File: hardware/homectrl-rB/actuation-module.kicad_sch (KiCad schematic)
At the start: 0 parts

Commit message: stepper driver circuitry
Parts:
- added C27: 2.2uF 6.3V, symbol Device:C
- added C28: 0.1uF 10V, symbol Device:C
- added C29: 22nF 50V, symbol Device:C
- added C30: 4.7uF 6.3V, symbol Device:C
- added C31, C32, C34: 0.1uF 24V, symbol Device:C
- added C33: 100uF 24V, symbol Device:C
- added D12, D13: S1M, symbol Device:D
- added J6: PUMP0-CONN, symbol Connector_Generic:Conn_01x02
- added J7: PUMP1-CONN, symbol Connector_Generic:Conn_01x02
- added J8: STEP-CONN, symbol Connector_Generic:Conn_01x04
- added Q2, Q3: IRLZ44N, IRLZ44N:TO254P1054X469X1930-3, symbol IRLZ44N:IRLZ44N
- added R21, R23, R27: 1k, symbol Device:R
- added R22, R24: 10k, symbol Device:R
- added R25, R26: 0.11, symbol Device:R
- added U8: TMC2209, QFN28_5X5_TRI, symbol TMC2209:TMC2209
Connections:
- new net: Q3.1, R23.2, R24.2
- new net: Q2.1, R21.2, R22.2
- new net: C29.1, U8.4 (CPO)
- new net: C29.2, U8.5 (CPI)
- new net: C27.1, C30.1, U8.8 (5VOUT)
- new net: R26.1, U8.23 (BRA)
- new net: R25.1, U8.27 (BRB)
- new net +12V: C31.1, C32.1, C33.1, C34.2, D12.1 (K), D13.1 (K), J6.1 (Pin_1), J7.1 (Pin_1), U8.22 (VS), U8.28 (VS), U8.6 (VCP)
- new net +3V3: C28.2, U8.10 (MS2_AD1), U8.15 (VCC_IO), U8.9 (MS1_AD0)
- new net 1A: J8.1 (Pin_1), U8.24 (OA1)
- new net 1B: J8.2 (Pin_2), U8.26 (OB1)
- new net 2A: J8.3 (Pin_3), U8.21 (OA2)
- new net 2B: J8.4 (Pin_4), U8.1 (OB2)
- new net DIR: U8.19 (DIR)
- new net ENN: U8.2 (ENN)
- new net GND: C27.2, C28.1, C30.2, C31.2, C32.2, C33.2, C34.1, Q2.3, Q3.3, R22.1, R24.1, R25.2, R26.2, U8.13 (CLK), U8.18 (GND), U8.29 (GND), U8.3 (GND), U8.7 (SPREAD)
- new net PGATE-0: R21.1
- new net PGATE-1: R23.1
- new net PUMP0-N: D12.2 (A), J6.2 (Pin_2), Q2.2
- new net PUMP1-N: D13.2 (A), J7.2 (Pin_2), Q3.2
- new net S3-RX: R27.2
- new net S3-TX: R27.1, U8.14 (PDN_UART)
- new net STEP: U8.16 (STEP)
- no-connect marks 0 -> 4
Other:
- note added: "+"
- note added: "-"
- note added: "A-IN"
- note added: "A-SW"
- note added: "STEP-DRV"

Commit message: assign footprints
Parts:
- C27: value 2.2uF 6.3V -> 2.2uF 10V; footprint (none) -> Capacitor_SMD:C_0201_0603Metric
- C28, C29: footprint (none) -> Capacitor_SMD:C_0603_1608Metric
- C30: value 4.7uF 6.3V -> 4.7uF 10V; footprint (none) -> Capacitor_SMD:C_0805_2012Metric
- C31, C32, C34: value 0.1uF 24V -> 0.1uF 50V; footprint (none) -> Capacitor_SMD:C_0603_1608Metric
- C33: value 100uF 24V -> 100uF 50V; footprint (none) -> Capacitor_SMD:CP_Elec_6.3x5.4
- D12: value S1M -> P0D; footprint (none) -> Diode_SMD:D_SMA
- D13: value S1M -> P1D; footprint (none) -> Diode_SMD:D_SMA
- J6, J7: footprint (none) -> 530480210:MOLEX_530480210
- J8: footprint (none) -> 530480410:MOLEX_530480410
- R21, R22, R23, R24: footprint (none) -> Resistor_SMD:R_0603_1608Metric
- R25, R26: footprint (none) -> Resistor_SMD:R_1206_3216Metric
- R27: footprint (none) -> Resistor_SMD:R_0402_1005Metric
- U8: footprint QFN28_5X5_TRI -> ul_TMC2209:QFN28_5X5_TRI
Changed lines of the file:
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@@
 			)
 		)
-		(property "Value" "S1M"
+		(property "Value" "P0D"
 			(at 39.37 38.1 0)
 			(effects
@@
 			)
 		)
-		(property "Footprint" ""
+		(property "Footprint" "Diode_SMD:D_SMA"
 			(at 39.37 41.91 0)
 			(effects
@@
 			)
 		)
-		(property "Footprint" ""
+		(property "Footprint" "Resistor_SMD:R_0603_1608Metric"
 			(at 87.63 65.278 90)
 			(effects
@@
 			)
 		)
-		(property "Footprint" ""
+		(property "Footprint" "Resistor_SMD:R_0603_1608Metric"
 			(at 41.91 65.278 90)
 			(effects
@@
 			)
 		)
-		(property "Footprint" ""
+		(property "Footprint" "Capacitor_SMD:C_0603_1608Metric"
 			(at 119.6848 142.24 0)
 			(effects
@@
 			)
 		)
-		(property "Value" "0.1uF 24V"
+		(property "Value" "0.1uF 50V"
 			(at 153.924 125.984 0)
 			(effects
@@
 			)
 		)
-		(property "Footprint" ""
+		(property "Footprint" "Capacitor_SMD:C_0603_1608Metric"
 			(at 155.9052 121.92 0)
 			(effects
@@
 			)
 		)
-		(property "Footprint" ""
+		(property "Footprint" "Resistor_SMD:R_0603_1608Metric"
 			(at 43.688 69.85 90)
 			(effects
@@
 			)
 		)
-		(property "Footprint" ""
+		(property "Footprint" "Capacitor_SMD:C_0603_1608Metric"
 			(at 58.1152 116.84 0)
 			(effects
@@
 			)
 		)
-		(property "Value" "0.1uF 24V"
+		(property "Value" "0.1uF 50V"
 			(at 142.748 125.984 0)
 			(effects
@@
 			)
 		)
-		(property "Footprint" ""
+		(property "Footprint" "Capacitor_SMD:C_0603_1608Metric"
 			(at 145.7452 121.92 0)
 			(effects
@@
 			)
 		)
-		(property "Value" "S1M"
+		(property "Value" "P1D"
 			(at 71.12 38.1 0)
 			(effects
@@
 			)
 		)
-		(property "Footprint" ""
+		(property "Footprint" "Diode_SMD:D_SMA"
 			(at 71.12 41.91 0)
 			(effects
@@
 			)
 		)
-		(property "Footprint" ""
+		(property "Footprint" "Resistor_SMD:R_0603_1608Metric"
 			(at 89.408 69.85 90)
 			(effects
@@
 			)
 		)
-		(property "Value" "2.2uF 6.3V"
+		(property "Value" "2.2uF 10V"
 			(at 37.338 126.238 0)
 			(effects
@@
 			)
 		)
-		(property "Footprint" ""
+		(property "Footprint" "Capacitor_SMD:C_0201_0603Metric"
 			(at 51.7652 129.54 0)
 			(effects
@@
 			)
 		)
-		(property "Footprint" ""
+		(property "Footprint" "530480210:MOLEX_530480210"
 			(at 69.85 27.94 0)
 			(effects
@@
 			)
 		)
-		(property "Footprint" ""
+		(property "Footprint" "530480410:MOLEX_530480410"
 			(at 101.6 27.94 0)
 			(effects
@@
 			)
 		)
-		(property "Value" "100uF 24V"
+		(property "Value" "100uF 50V"
 			(at 168.656 119.38 0)
 			(effects
@@
 			)
 		)
-		(property "Footprint" ""
+		(property "Footprint" "Capacitor_SMD:CP_Elec_6.3x5.4"
 			(at 166.0652 121.92 0)
 			(effects
@@
 			)
 		)
-		(property "Value" "0.1uF 24V"
+		(property "Value" "0.1uF 50V"
 			(at 33.528 113.538 0)
 			(effects
@@
 			)
 		)
-		(property "Footprint" ""
+		(property "Footprint" "Capacitor_SMD:C_0603_1608Metric"
 			(at 47.9552 116.84 0)
 			(effects
@@
 			)
 		)
-		(property "Footprint" ""
+		(property "Footprint" "530480210:MOLEX_530480210"
 			(at 38.1 27.94 0)
 			(effects
@@
 			)
 		)
-		(property "Footprint" "QFN28_5X5_TRI"
+		(property "Footprint" "ul_TMC2209:QFN28_5X5_TRI"
 			(at 69.85 104.14 0)
 			(effects
@@
 			)
 		)
-		(property "Footprint" ""
+		(property "Footprint" "Resistor_SMD:R_1206_3216Metric"
 			(at 124.46 121.158 90)
 			(effects
@@
 			)
 		)
-		(property "Footprint" ""
+		(property "Footprint" "Resistor_SMD:R_0402_1005Metric"
 			(at 59.182 140.97 90)
 			(effects
@@
 			)
 		)
-		(property "Value" "4.7uF 6.3V"
+		(property "Value" "4.7uF 10V"
 			(at 37.084 131.572 0)
 			(effects
@@
 			)
 		)
-		(property "Footprint" ""
+		(property "Footprint" "Capacitor_SMD:C_0805_2012Metric"
 			(at 58.1152 129.54 0)
 			(effects
@@
 			)
 		)
-		(property "Footprint" ""
+		(property "Footprint" "Resistor_SMD:R_1206_3216Metric"
 			(at 124.46 110.998 90)
 			(effects

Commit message: layout work
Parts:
- C27: footprint Capacitor_SMD:C_0201_0603Metric -> Capacitor_SMD:C_0603_1608Metric
- Q2, Q3: footprint IRLZ44N:TO254P1054X469X1930-3 -> Package_TO_SOT_SMD:SOT-23
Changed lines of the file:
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@@
 			)
 		)
-		(property "Footprint" "IRLZ44N:TO254P1054X469X1930-3"
+		(property "Footprint" "Package_TO_SOT_SMD:SOT-23"
 			(at 48.26 60.96 0)
 			(effects
@@
 			)
 		)
-		(property "Footprint" "Capacitor_SMD:C_0201_0603Metric"
+		(property "Footprint" "Capacitor_SMD:C_0603_1608Metric"
 			(at 51.7652 129.54 0)
 			(effects
@@
 			)
 		)
-		(property "Footprint" "IRLZ44N:TO254P1054X469X1930-3"
+		(property "Footprint" "Package_TO_SOT_SMD:SOT-23"
 			(at 93.98 60.96 0)
 			(effects

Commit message: W
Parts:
- C27, C28, C29, C30, C31, C32, C33, C34, D12, D13, Q2, Q3, U8: Purchase (none) -> Yes
- J6, J7, J8: Purchase (none) -> No
- R21, R22, R23, R24, R25, R26, R27: Purchase (none) -> N/A

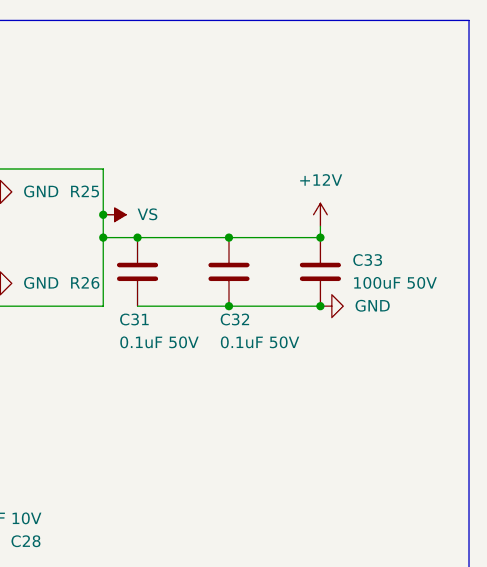
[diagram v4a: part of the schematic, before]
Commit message: add new caps, add ferrite bead, add MPNs
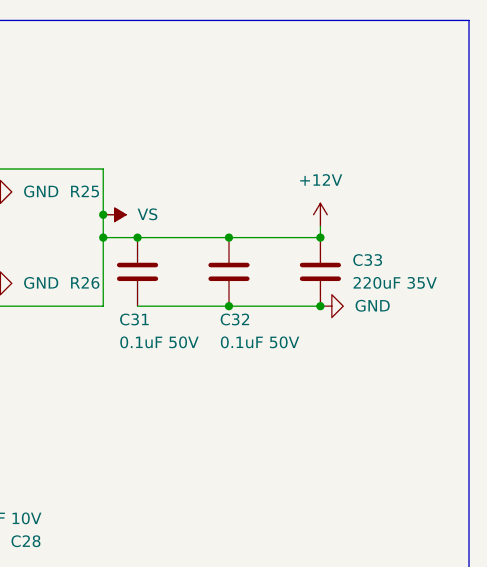
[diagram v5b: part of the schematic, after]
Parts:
- C33: value 100uF 50V -> 220uF 35V; footprint Capacitor_SMD:CP_Elec_6.3x5.4 -> EEE_FK1V101P:CAP_EEEFK1V101P; MPN (none) -> EEE-FK1V221P
- J6, J7, J8: MPN (none) -> N/A
- R21, R22, R23, R24, R25, R26, R27: Purchase N/A -> Yes
- U8: MPN (none) -> TMC2209-LA-T
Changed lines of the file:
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@@
 			)
 		)
-		(property "Purchase" "N/A"
+		(property "Purchase" "Yes"
 			(at 87.63 63.5 0)
 			(effects
@@
 			)
 		)
-		(property "Purchase" "N/A"
+		(property "Purchase" "Yes"
 			(at 41.91 63.5 0)
 			(effects
@@
 			)
 		)
-		(property "Purchase" "N/A"
+		(property "Purchase" "Yes"
 			(at 41.91 69.85 0)
 			(effects
@@
 			)
 		)
-		(property "Purchase" "N/A"
+		(property "Purchase" "Yes"
 			(at 87.63 69.85 0)
 			(effects
@@
 			)
 		)
-		(property "MPN" ""
+		(property "MPN" "N/A"
 			(at 69.85 27.94 0)
 			(effects
@@
 			)
 		)
-		(property "MPN" ""
+		(property "MPN" "N/A"
 			(at 101.6 27.94 0)
 			(effects
@@
 			)
 		)
-		(property "Value" "100uF 50V"
+		(property "Value" "220uF 35V"
 			(at 168.656 119.38 0)
 			(effects
@@
 			)
 		)
-		(property "Footprint" "Capacitor_SMD:CP_Elec_6.3x5.4"
+		(property "Footprint" "EEE_FK1V101P:CAP_EEEFK1V101P"
 			(at 166.0652 121.92 0)
 			(effects
@@
 			)
 		)
-		(property "MPN" ""
+		(property "MPN" "EEE-FK1V221P"
 			(at 165.1 118.11 0)
 			(effects
@@
 			)
 		)
-		(property "MPN" ""
+		(property "MPN" "N/A"
 			(at 38.1 27.94 0)
 			(effects
@@
 			)
 		)
-		(property "MPN" ""
+		(property "MPN" "TMC2209-LA-T"
 			(at 69.85 104.14 0)
 			(effects
@@
 			)
 		)
-		(property "Purchase" "N/A"
+		(property "Purchase" "Yes"
 			(at 124.46 119.38 0)
 			(effects
@@
 			)
 		)
-		(property "Purchase" "N/A"
+		(property "Purchase" "Yes"
 			(at 60.96 140.97 0)
 			(effects
@@
 			)
 		)
-		(property "Purchase" "N/A"
+		(property "Purchase" "Yes"
 			(at 124.46 109.22 0)
 			(effects

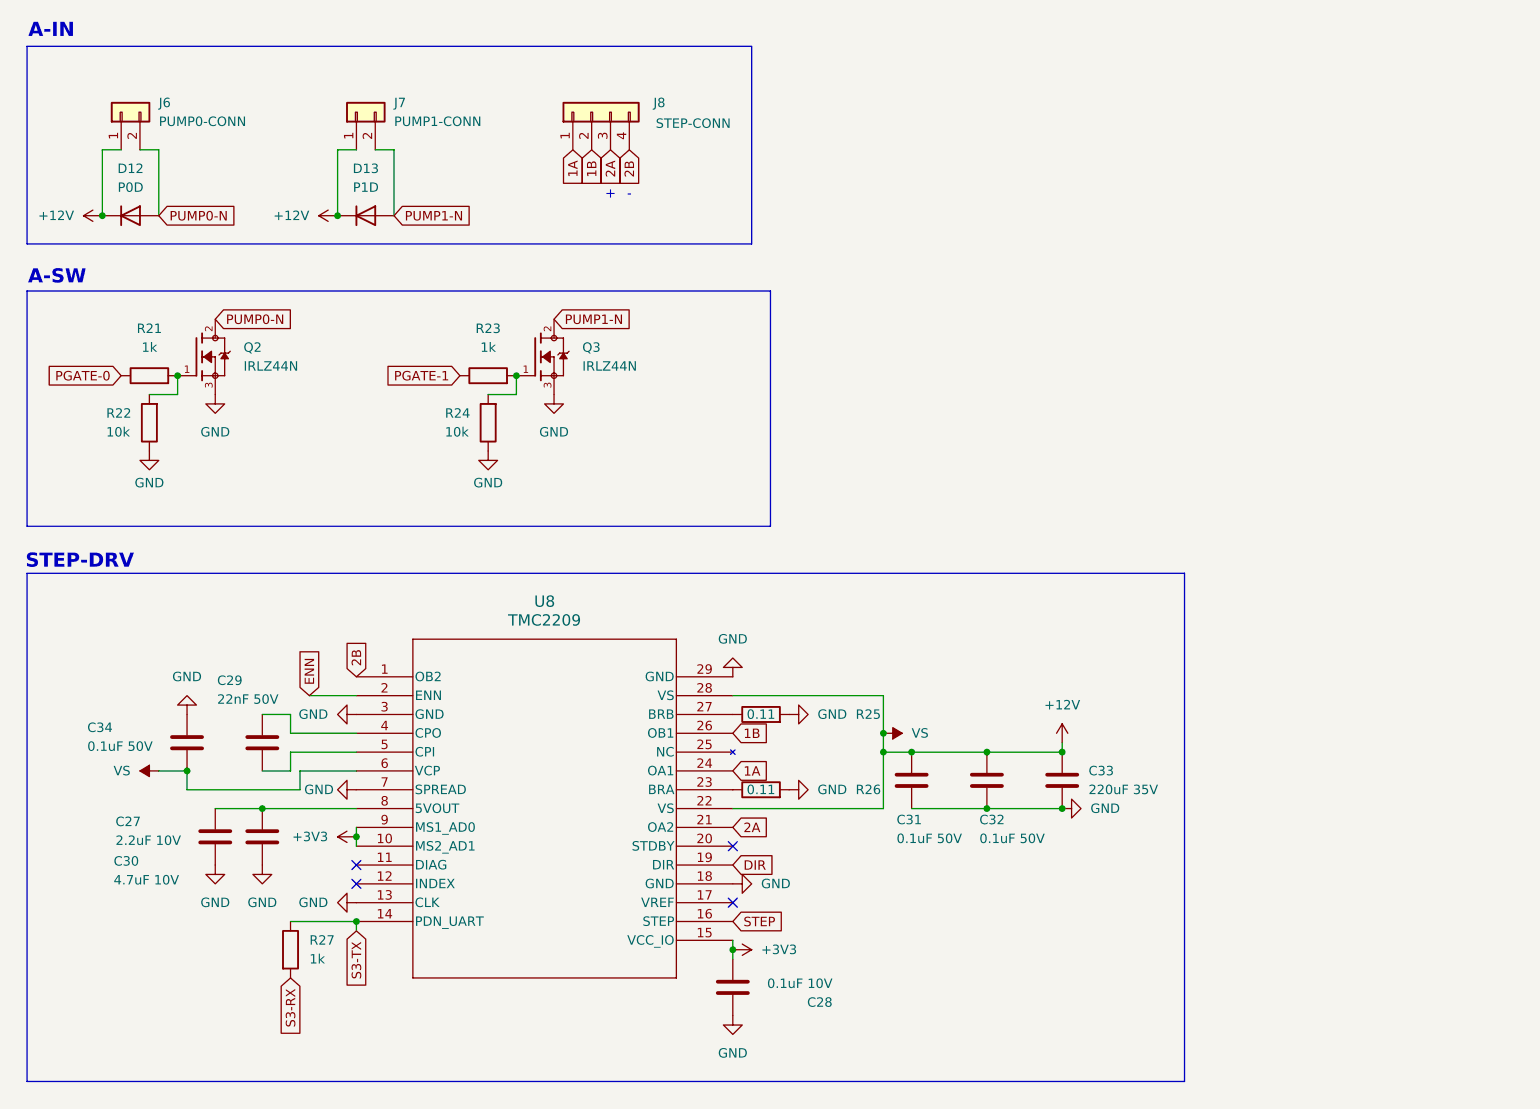
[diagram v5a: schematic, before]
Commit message: add MPNs and review circuits
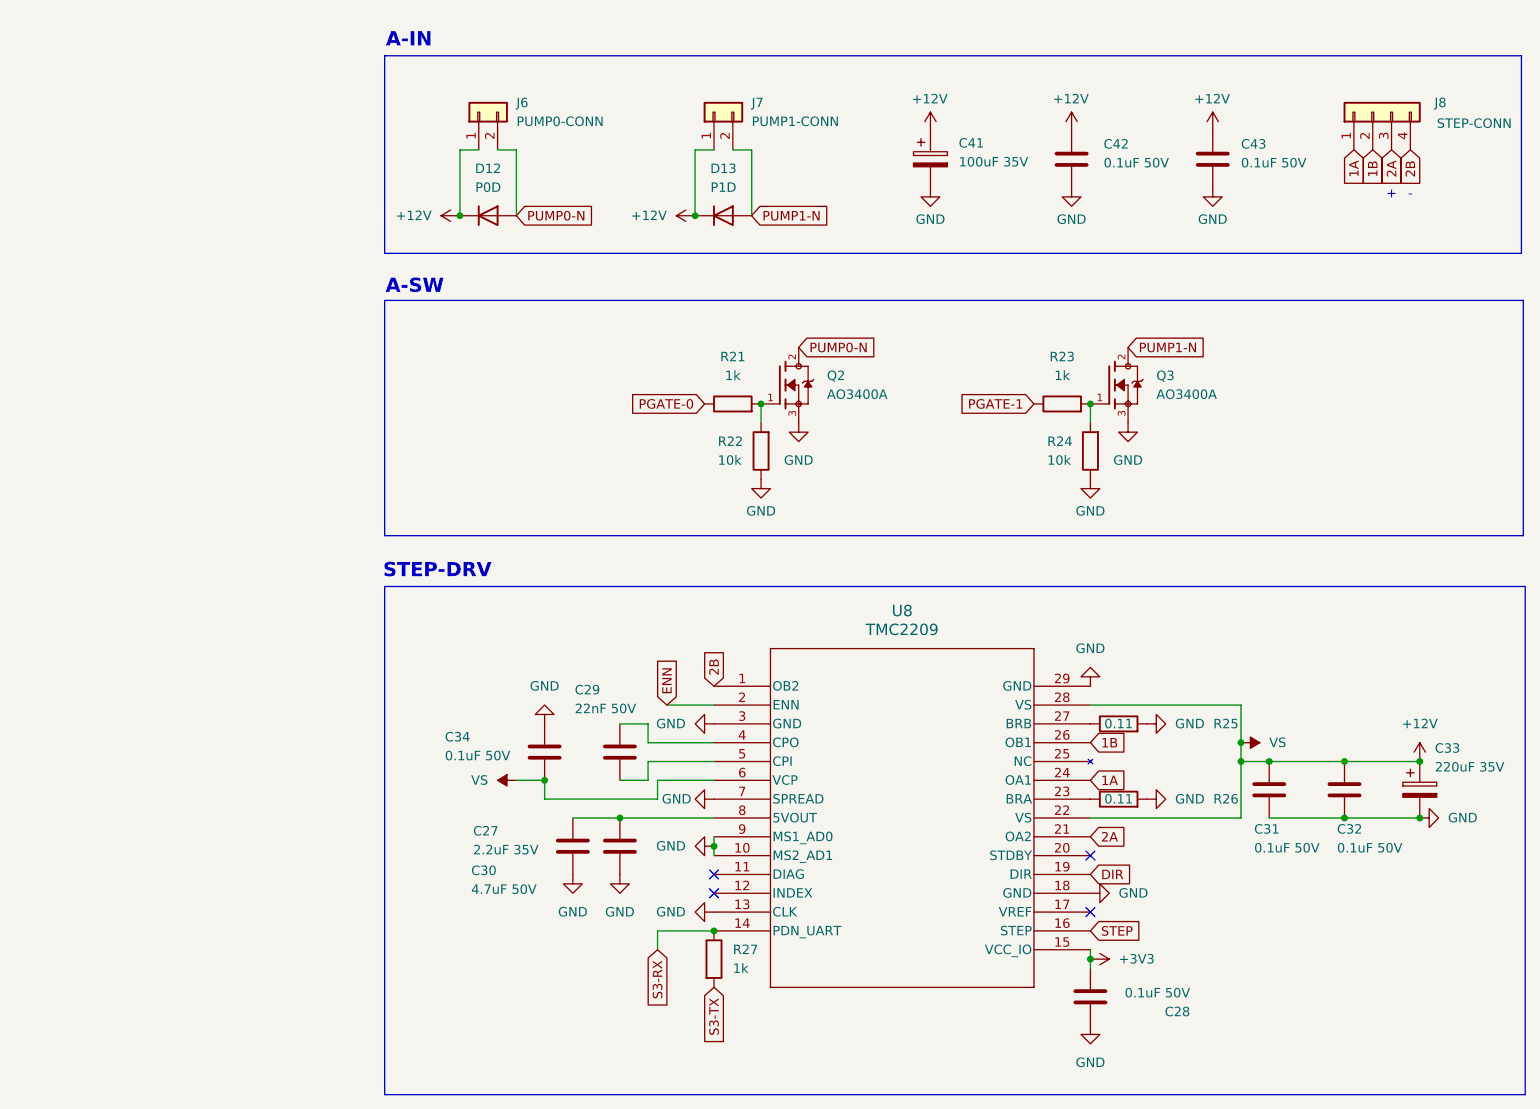
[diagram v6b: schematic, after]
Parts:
- added C41: 100uF 35V, EEH_ZK1V101XP:CAP_EEHZK1V101XP, symbol Device:C_Polarized
- added C42, C43: 0.1uF 50V, Capacitor_SMD:C_0603_1608Metric, symbol Device:C
- C27: value 2.2uF 10V -> 2.2uF 35V; MPN (none) -> https://www.digikey.ca/en/products/detail/murata-electronic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
- C28: value 0.1uF 10V -> 0.1uF 50V; MPN (none) -> GRM188R71H104KA93D
- C29: MPN (none) -> CL10B223KB8NNNC
- C30: value 4.7uF 10V -> 4.7uF 50V; MPN (none) -> CL21A475KBQNNNE
- C31, C32, C34: MPN (none) -> GRM188R71H104KA93D
- C33: symbol Device:C -> Device:C_Polarized
- D12, D13: MPN (none) -> SS14
- Q2: value IRLZ44N -> AO3400A; MPN (none) -> AO3400A
- Q3: value IRLZ44N -> AO3400A; MP IRLZ44N -> (none); MPN (none) -> AO3400A
- R21: MPN (none) -> ERJ-3EKF1001V
- R22, R24: MPN (none) -> ERJ-3EKF1002V
- R23: MPN (none) -> https://industrial.panasonic.com/cdbs/www-data/pdf/RDA0000/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
- R25, R26: MPN (none) -> RL1206FR-070R11L
- R27: MPN (none) -> ERJ-2RKF1001X
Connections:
- net +12V: now also C41.1, C42.1, C43.1
- net +3V3: no longer U8.10 (MS2_AD1), U8.9 (MS1_AD0)
- net GND: now also U8.10 (MS2_AD1), U8.9 (MS1_AD0), C41.2, C42.2, C43.2
- net S3-RX: now also R27.1, U8.14 (PDN_UART); no longer R27.2
- net S3-TX: now also R27.2; no longer R27.1, U8.14 (PDN_UART)
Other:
- moved on the sheet: C27, C28, C29, C30, C31, C32, C34, D12, D13, J6, J7, J8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

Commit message: pad clearance & BOM fixes
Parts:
- C28, C31, C32, C34, C42, C43: MPN GRM188R71H104KA93D -> CC0603KRX7R9BB104
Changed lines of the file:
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@@
 			)
 		)
-		(property "MPN" "GRM188R71H104KA93D"
+		(property "MPN" "CC0603KRX7R9BB104"
 			(at 168.91 147.32 0)
 			(effects
@@
 			)
 		)
-		(property "MPN" "GRM188R71H104KA93D"
+		(property "MPN" "CC0603KRX7R9BB104"
 			(at 203.2 119.38 0)
 			(effects
@@
 			)
 		)
-		(property "MPN" "GRM188R71H104KA93D"
+		(property "MPN" "CC0603KRX7R9BB104"
 			(at 193.04 119.38 0)
 			(effects
@@
 			)
 		)
-		(property "MPN" "GRM188R71H104KA93D"
+		(property "MPN" "CC0603KRX7R9BB104"
 			(at 185.42 34.29 0)
 			(effects
@@
 			)
 		)
-		(property "MPN" "GRM188R71H104KA93D"
+		(property "MPN" "CC0603KRX7R9BB104"
 			(at 95.25 114.3 0)
 			(effects
@@
 			)
 		)
-		(property "MPN" "GRM188R71H104KA93D"
+		(property "MPN" "CC0603KRX7R9BB104"
 			(at 166.37 34.29 0)
 			(effects

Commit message: swap connector in progress
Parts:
- C27: value 2.2uF 35V -> 2.2uF
- C28, C31, C32, C34, C42, C43: value 0.1uF 50V -> 0.1uF
- C29: value 22nF 50V -> 22nF
- C30: value 4.7uF 50V -> 4.7uF
- C33: value 220uF 35V -> 220uF; Comments (none) -> EEE-FK1V221P is the correct MPN even though the footprint h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
- C41: value 100uF 35V -> 100uF; MPN UWT1V101MCL1GS -> EEH-ZK1V101XP
- D12, D13: Comments (none) -> onsemi
- J6, J7: footprint 530480210:MOLEX_530480210 -> S02B_PASK_2:CONN2_S02B-PASK-2_JST
- J8: footprint 530480410:MOLEX_530480410 -> S04B_PASK_2:CONN4_S04B-PASK_JST
- Q2, Q3: Comments (none) -> Confirmed AO3400A , brand:AOS,package:SOT-23-3L
- R23: MPN https://industrial.panasonic.com/cdbs/www-data/pdf/RDA0000/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 -> ERJ-3EKF1001V
